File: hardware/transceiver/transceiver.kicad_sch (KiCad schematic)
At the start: 48 parts, among them J1 Conn_01x04, J2 Conn_01x02, J3 Conn_Coaxial, J4 Conn_01x02, U1 SX1262IMLTRT, U2 AP2112K-3.3, U3 PE4259, U4 STM32U585CIUx, Y1 32MHz, Y2 Q13FC13500004, Y3 X322516MLB4SI

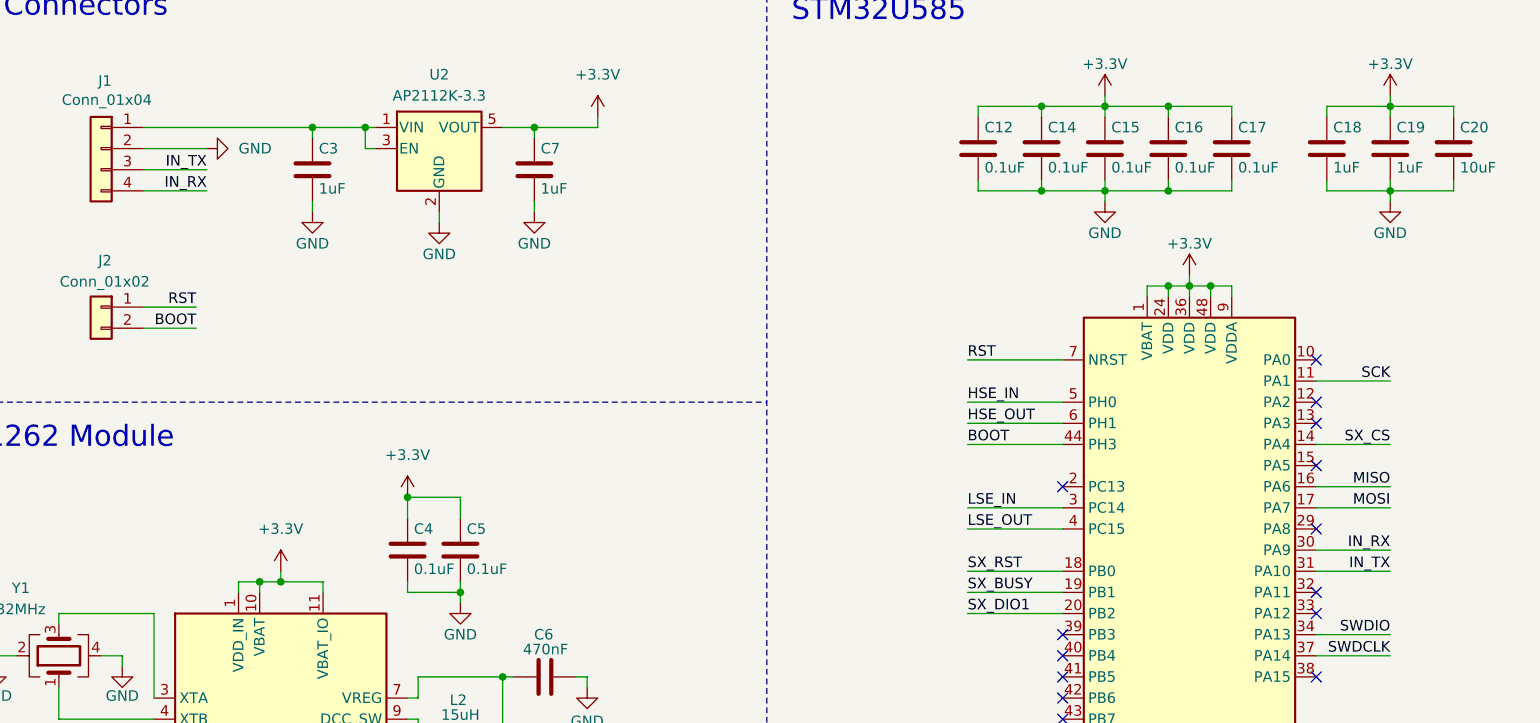
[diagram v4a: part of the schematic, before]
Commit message: changed boot1 and reset1 to boot and reset
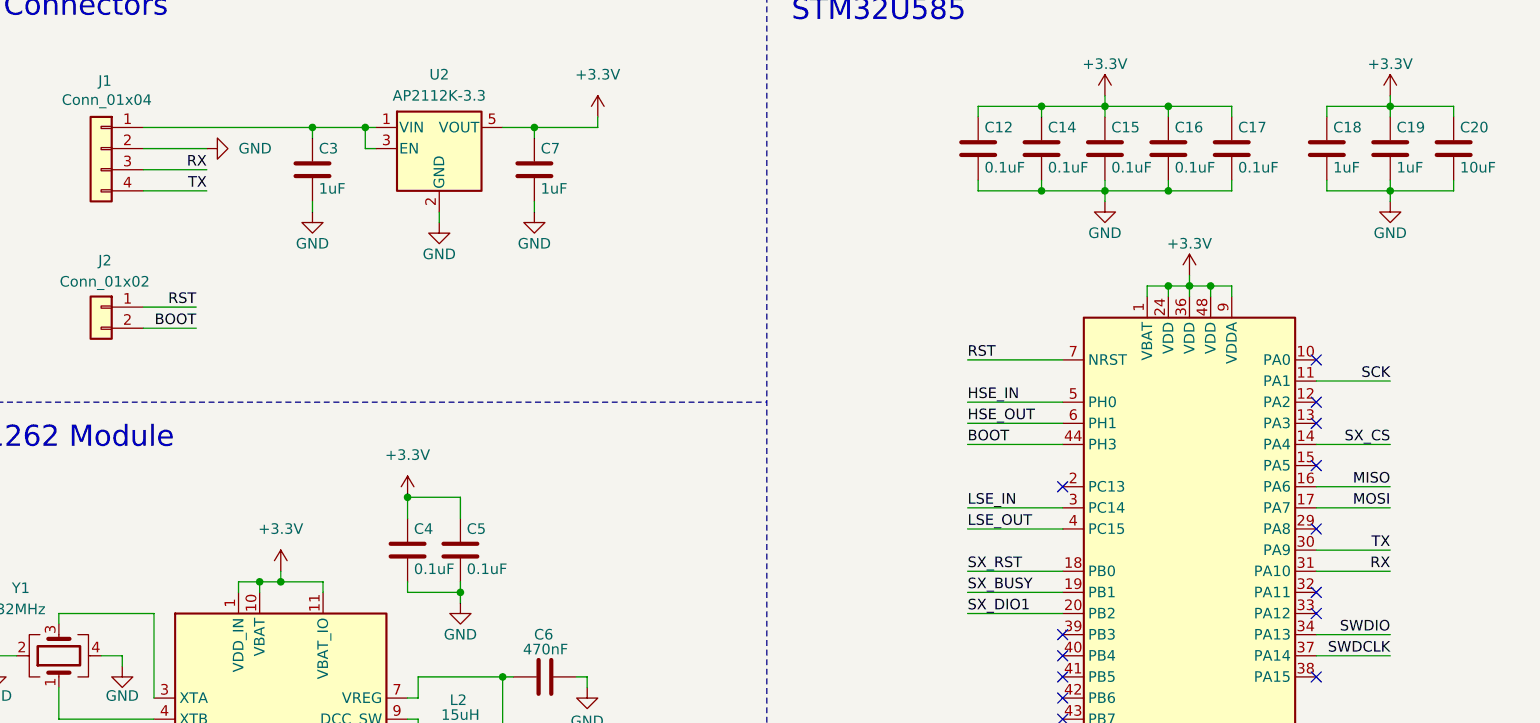
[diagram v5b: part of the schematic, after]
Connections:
- net IN_RX renamed TX
- net IN_TX renamed RX
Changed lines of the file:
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@@
 		)
 	)
-	(label "IN_RX"
+	(label "TX"
 		(at 187.96 81.28 180)
 		(effects
@@
 		)
 	)
-	(label "IN_RX"
+	(label "TX"
 		(at 45.72 38.1 180)
 		(effects
@@
 		)
 	)
-	(label "IN_TX"
+	(label "RX"
 		(at 187.96 83.82 180)
 		(effects
@@
 		)
 	)
-	(label "IN_TX"
+	(label "RX"
 		(at 45.72 35.56 180)
 		(effects

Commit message: added production files
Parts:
- BOOT1: value Boot -> SW_Push
- L2: footprint Inductor_SMD:L_0402_1005Metric -> Inductor_SMD:L_0603_1608Metric
- R2, R3: value 1k -> 2K
- RESET1: value Reset -> SW_Push
- renumbered C7 to C6, C6 to C7
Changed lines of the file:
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@@
 		(on_board yes)
 		(dnp no)
-		(property "Reference" "C7"
+		(property "Reference" "C6"
 			(at 85.852 33.02 0)
 			(effects
@@
 			(project "transceiver"
 				(path "/90219c92-b6dc-438d-9fd1-0abd4c4047d3"
-					(reference "C7")
+					(reference "C6")
 					(unit 1)
 				)
@@
 			)
 		)
-		(property "Value" "Boot"
+		(property "Value" "SW_Push"
 			(at 252.73 101.6 0)
 			(effects
@@
 		(dnp no)
 		(fields_autoplaced yes)
-		(property "Reference" "#PWR023"
+		(property "Reference" "#PWR022"
 			(at 140.97 187.96 0)
 			(effects
@@
 			(project ""
 				(path "/90219c92-b6dc-438d-9fd1-0abd4c4047d3"
-					(reference "#PWR023")
+					(reference "#PWR022")
 					(unit 1)
 				)
@@
 			)
 		)
-		(property "Value" "1k"
+		(property "Value" "2K"
 			(at 123.825 112.649 0)
 			(effects
@@
 		(on_board yes)
 		(dnp no)
-		(property "Reference" "#PWR010"
+		(property "Reference" "#PWR011"
 			(at 76.2 93.98 0)
 			(effects
@@
 			(project "transceiver"
 				(path "/90219c92-b6dc-438d-9fd1-0abd4c4047d3"
-					(reference "#PWR010")
+					(reference "#PWR011")
 					(unit 1)
 				)
@@
 			)
 		)
-		(property "Value" "Reset"
+		(property "Value" "SW_Push"
 			(at 229.87 101.6 0)
 			(effects
@@
 		(on_board yes)
 		(dnp no)
-		(property "Reference" "C6"
+		(property "Reference" "C7"
 			(at 87.376 91.44 90)
 			(effects
@@
 			(project "transceiver"
 				(path "/90219c92-b6dc-438d-9fd1-0abd4c4047d3"
-					(reference "C6")
+					(reference "C7")
 					(unit 1)
 				)
@@
 		(on_board yes)
 		(dnp no)
-		(property "Reference" "#PWR022"
+		(property "Reference" "#PWR023"
 			(at 143.51 140.97 0)
 			(effects
@@
 			(project "transceiver"
 				(path "/90219c92-b6dc-438d-9fd1-0abd4c4047d3"
-					(reference "#PWR022")
+					(reference "#PWR023")
 					(unit 1)
 				)
@@
 			)
 		)
-		(property "Footprint" "Inductor_SMD:L_0402_1005Metric"
+		(property "Footprint" "Inductor_SMD:L_0603_1608Metric"
 			(at 76.2 102.87 0)
 			(effects
@@
 		(on_board yes)
 		(dnp no)
-		(property "Reference" "#PWR011"
+		(property "Reference" "#PWR010"
 			(at 73.66 48.26 0)
 			(effects
@@
 			(project "transceiver"
 				(path "/90219c92-b6dc-438d-9fd1-0abd4c4047d3"
-					(reference "#PWR011")
+					(reference "#PWR010")
 					(unit 1)
 				)
@@
 			)
 		)
-		(property "Value" "1k"
+		(property "Value" "2K"
 			(at 133.985 112.649 0)
 			(effects
